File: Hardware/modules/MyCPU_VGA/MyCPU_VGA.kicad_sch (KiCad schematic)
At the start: 18 parts, among them J1 Bus_PCI_6502, J2 MyCPU Bus, U1 74HC138, U2 74HC138, U3 74AHC541, U4 74HCT574, U5 74HCT574, U6 74HCT574, U7 74HC00, U8 74HC02

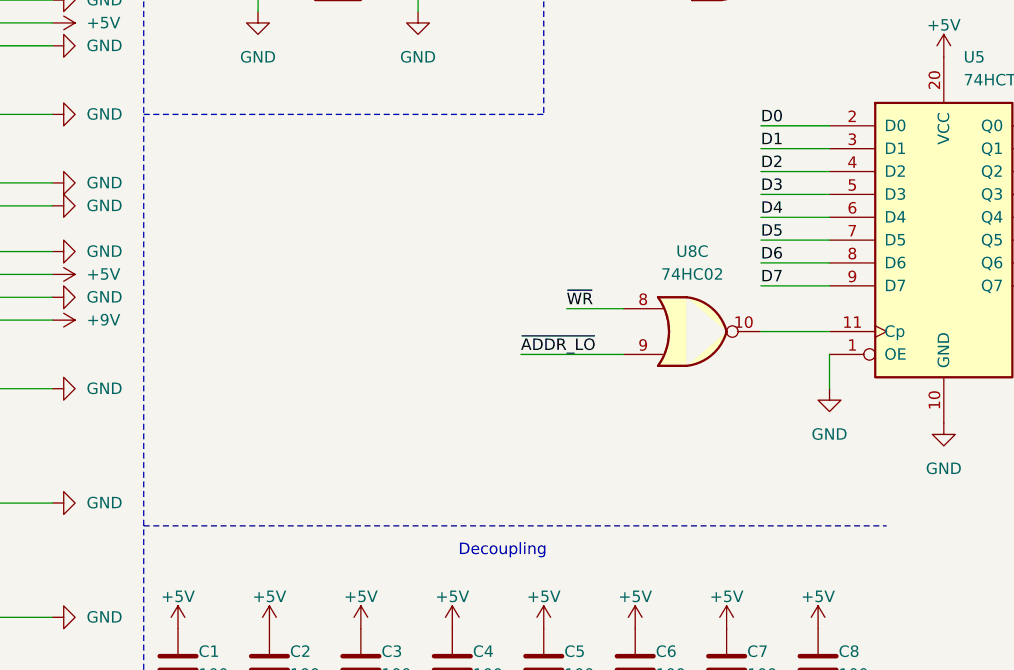
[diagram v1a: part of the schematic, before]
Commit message: Hardware Review Pt. 1 fix Address Decoding for Strobe Generators add bulk capacitance to every board fix wiring of Prototyping Board
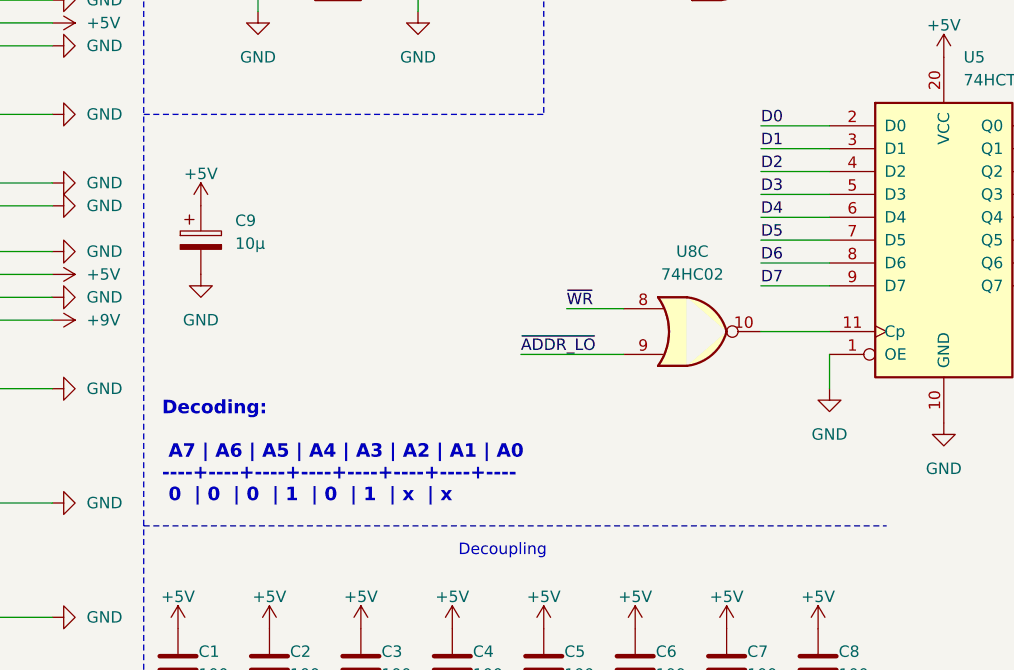
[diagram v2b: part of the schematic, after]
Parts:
- added C9: 10µ, Capacitor_THT:CP_Radial_D5.0mm_P2.50mm, symbol Device:C_Polarized
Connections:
- net +5V: now also C9.1
- net GND: now also C9.2
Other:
- note added: "Decoding: A7 | A6 | A5 | A4 | A3 | A2 | A1 | A0 ----+----+----+----+----+----+----+---- 0 | 0 | 0 | 1 | 0 | 1 | x | x"
